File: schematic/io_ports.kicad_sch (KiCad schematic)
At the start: 4 parts, among them J1 Cartridge Port, J2 Expansion Port

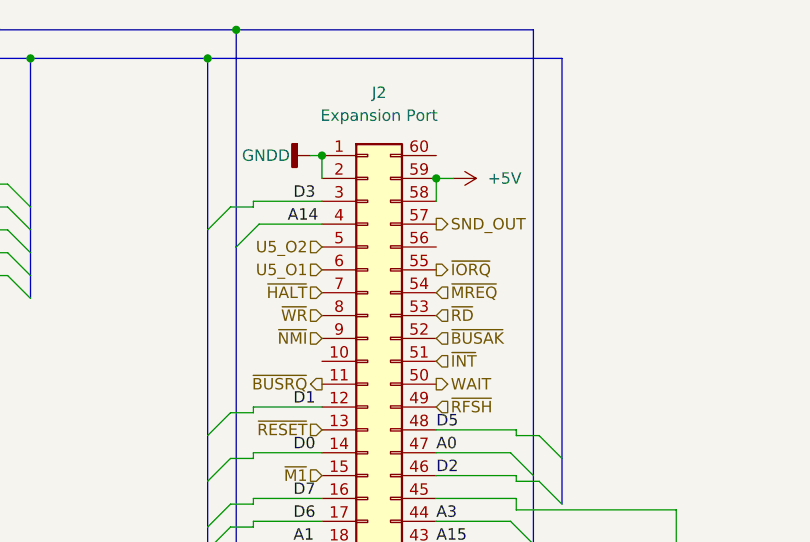
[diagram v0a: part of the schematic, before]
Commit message: power supply added, controller circuit added. Controller is a very odd duck to say the least. Seems they wanted to have plenty of current, maybe due to the steering wheel attachement?
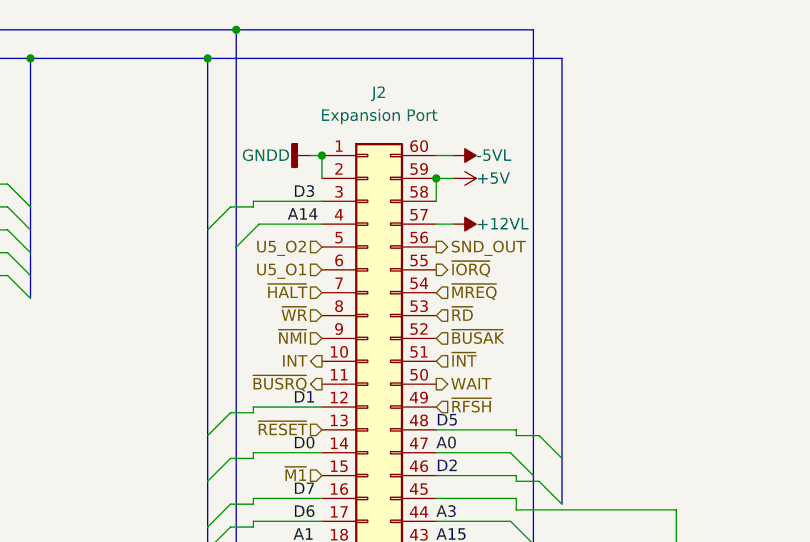
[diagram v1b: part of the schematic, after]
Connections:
- net SND_OUT: now also J2.56 (Pin_56); no longer J2.57 (Pin_57)
- net INT: now reaches J2.10 (Pin_10)
- net -5VL: now reaches J2.60 (Pin_60)
- new net +12VL: J2.57 (Pin_57)
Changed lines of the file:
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@@
+    (stroke (width 0) (type default) (color 0 0 0 0))
+  )
+  (wire (pts (xy 177.8 54.61) (xy 175.895 54.61))
     (stroke (width 0) (type default) (color 0 0 0 0))
   )
@@
     (stroke (width 0) (type default) (color 0 0 0 0))
   )
+  (wire (pts (xy 175.895 46.99) (xy 177.8 46.99))
+    (stroke (width 0) (type default) (color 0 0 0 0))
+  )
   (bus (pts (xy 153.67 102.87) (xy 153.67 105.41))
     (stroke (width 0) (type default) (color 0 0 0 0))
@@
     (effects (font (size 1.27 1.27)) (justify right))
   )
+  (hierarchical_label "INT" (shape output) (at 163.195 69.85 180)
+    (effects (font (size 1.27 1.27)) (justify right))
+  )
   (hierarchical_label "E3_U5" (shape output) (at 144.145 118.745 180)
     (effects (font (size 1.27 1.27)) (justify right))
@@
     (effects (font (size 1.27 1.27)) (justify left))
   )
-  (hierarchical_label "SND_OUT" (shape output) (at 175.895 54.61 0)
+  (hierarchical_label "SND_OUT" (shape output) (at 175.895 57.15 0)
     (effects (font (size 1.27 1.27)) (justify left))
   )
@@
   )
   (symbol (lib_id "power:+5V") (at 177.8 49.53 270) (unit 1)
-    (in_bom yes) (on_board yes) (fields_autoplaced)
+    (in_bom yes) (on_board yes)
     (property "Reference" "#PWR?" (id 0) (at 173.99 49.53 0)
       (effects (font (size 1.27 1.27)) hide)
     )
-    (property "Value" "+5V" (id 1) (at 181.61 49.5299 90)
+    (property "Value" "+5V" (id 1) (at 180.34 49.53 90)
       (effects (font (size 1.27 1.27)) (justify left))
     )
@@
     (pin "2")
   )
+  (symbol (lib_id "Power_Symbols:-5VL") (at 177.8 46.99 270) (unit 1)
+    (in_bom yes) (on_board yes)
+    (property "Reference" "#PWR?" (id 0) (at 180.34 46.99 0)
+      (effects (font (size 1.27 1.27)) hide)
+    )
+    (property "Value" "-5VL" (id 1) (at 180.34 46.99 90)
+      (effects (font (size 1.27 1.27)) (justify left))
+    )
+    (property "Footprint" "" (id 2) (at 177.8 46.99 0)
+      (effects (font (size 1.27 1.27)) hide)
+    )
+    (property "Datasheet" "" (id 3) (at 177.8 46.99 0)
+      (effects (font (size 1.27 1.27)) hide)
+    )
+    (pin "1")
+  )
   (symbol (lib_id "power:+5V") (at 117.475 83.185 180) (unit 1)
     (in_bom yes) (on_board yes) (fields_autoplaced)
@@
       (effects (font (size 1.27 1.27)) hide)
     )
+    (pin "1")
+  )
+  (symbol (lib_id "Power_Symbols:+12VL") (at 177.8 54.61 270) (unit 1)
+    (in_bom yes) (on_board yes)
+    (property "Reference" "#PWR?" (id 0) (at 180.34 54.61 0)
+      (effects (font (size 1.27 1.27)) hide)
+    )
+    (property "Value" "+12VL" (id 1) (at 180.34 54.61 90)
+      (effects (font (size 1.27 1.27)) (justify left))
+    )
+    (property "Footprint" "" (id 2) (at 177.8 54.61 0)
+      (effects (font (size 1.27 1.27)) hide)
+    )
+    (property "Datasheet" "" (id 3) (at 177.8 54.61 0)
+      (effects (font (size 1.27 1.27)) hide)
+    )

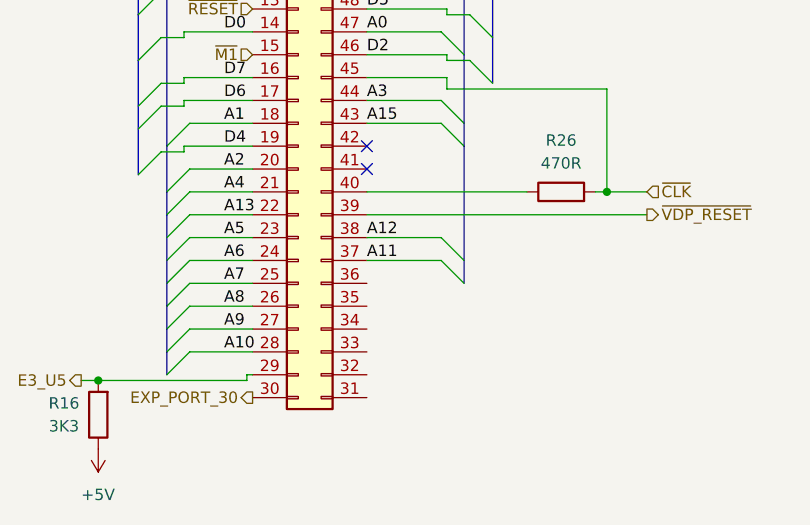
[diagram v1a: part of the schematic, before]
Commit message: started work on clock_reset_misc circuits. inverter u7 done, u8 added and starting work around U22.
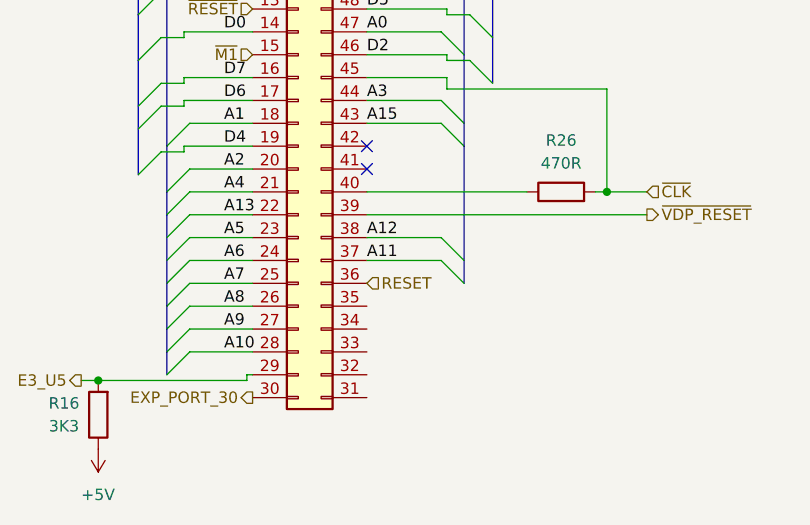
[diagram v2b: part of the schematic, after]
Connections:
- net RESET: now reaches J2.36 (Pin_36)
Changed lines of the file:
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@@
+    (effects (font (size 1.27 1.27)) (justify left))
+  )
+  (hierarchical_label "RESET" (shape input) (at 175.895 107.95 0)
     (effects (font (size 1.27 1.27)) (justify left))
   )

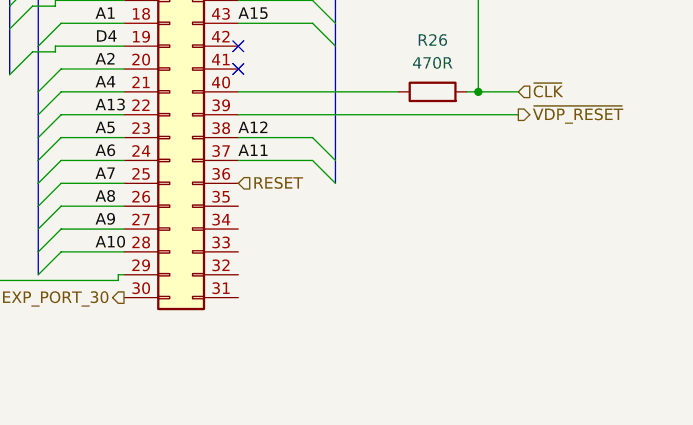
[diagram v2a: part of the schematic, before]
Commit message: altered and did some cleanup of the way the wires were run. Finished expansion port routes to rf modulator. Added ext_psu for future external power supply design (will be an off the shelf psu block).
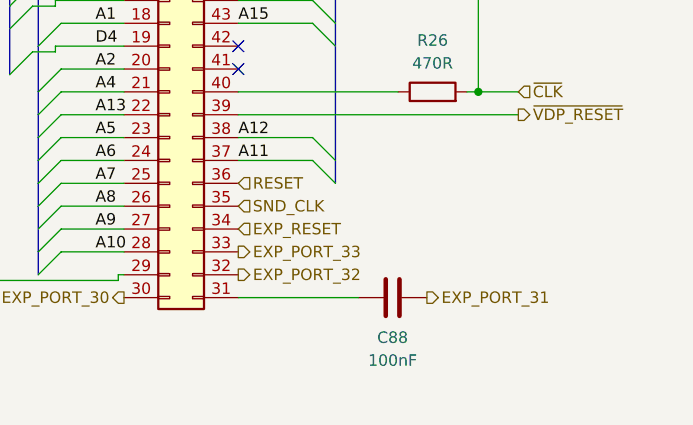
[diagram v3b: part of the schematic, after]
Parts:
- added C88: 100nF, symbol Device:C
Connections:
- net at J2.31 (Pin_31): now also C88.1
- net EXP_PORT_32: now reaches J2.32 (Pin_32)
- net EXP_PORT_33: now reaches J2.33 (Pin_33)
- net EXP_RESET: now reaches J2.34 (Pin_34)
- net SND_CLK: now reaches J2.35 (Pin_35)
- new net EXP_PORT_31: C88.2
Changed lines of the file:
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@@
+    (stroke (width 0) (type default) (color 0 0 0 0))
+  )
+  (wire (pts (xy 175.895 120.65) (xy 189.23 120.65))
     (stroke (width 0) (type default) (color 0 0 0 0))
   )
@@
     (effects (font (size 1.27 1.27)) (justify right))
   )
+  (hierarchical_label "EXP_PORT_32" (shape output) (at 175.895 118.11 0)
+    (effects (font (size 1.27 1.27)) (justify left))
+  )
   (hierarchical_label "~{NMI}" (shape input) (at 163.195 67.31 180)
     (effects (font (size 1.27 1.27)) (justify right))
@@
     (effects (font (size 1.27 1.27)) (justify right))
   )
+  (hierarchical_label "EXP_PORT_31" (shape output) (at 196.85 120.65 0)
+    (effects (font (size 1.27 1.27)) (justify left))
+  )
   (hierarchical_label "INT" (shape output) (at 163.195 69.85 180)
     (effects (font (size 1.27 1.27)) (justify right))
@@
     (effects (font (size 1.27 1.27)) (justify right))
   )
+  (hierarchical_label "EXP_RESET" (shape input) (at 175.895 113.03 0)
+    (effects (font (size 1.27 1.27)) (justify left))
+  )
   (hierarchical_label "U5_O4" (shape input) (at 117.475 67.945 0)
     (effects (font (size 1.27 1.27)) (justify left))
   )
+  (hierarchical_label "SND_CLK" (shape input) (at 175.895 110.49 0)
+    (effects (font (size 1.27 1.27)) (justify left))
+  )
   (hierarchical_label "~{CLK}" (shape input) (at 207.01 97.79 0)
+    (effects (font (size 1.27 1.27)) (justify left))
+  )
+  (hierarchical_label "EXP_PORT_33" (shape output) (at 175.895 115.57 0)
     (effects (font (size 1.27 1.27)) (justify left))
   )
@@
     (pin "1")
   )
+  (symbol (lib_id "Device:C") (at 193.04 120.65 90) (unit 1)
+    (in_bom yes) (on_board yes)
+    (property "Reference" "C88" (id 0) (at 193.04 125.095 90))
+    (property "Value" "100nF" (id 1) (at 193.04 127.635 90))
+    (property "Footprint" "" (id 2) (at 196.85 119.6848 0)
+      (effects (font (size 1.27 1.27)) hide)
+    )
+    (property "Datasheet" "~" (id 3) (at 193.04 120.65 0)
+      (effects (font (size 1.27 1.27)) hide)
+    )
+    (pin "1")
+    (pin "2")
+  )
   (symbol (lib_id "Power_Symbols:+12VL") (at 177.8 54.61 270) (unit 1)

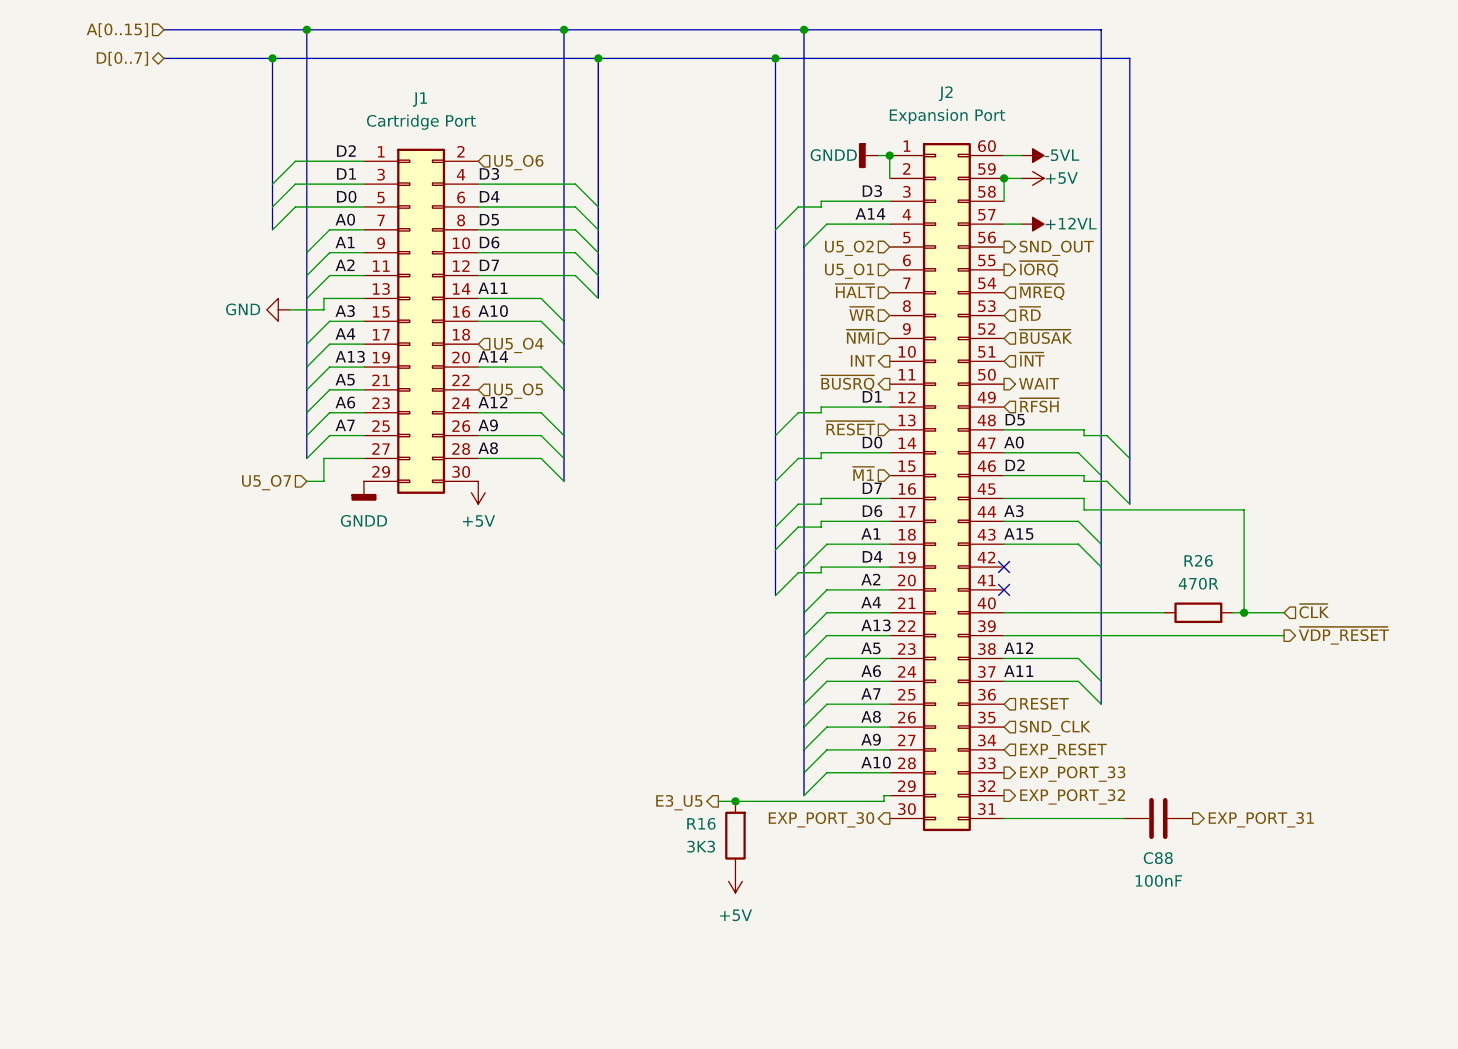
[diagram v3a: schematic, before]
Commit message: cleanup of power supply, and another pass at the RF circuit. Both look much better. The RF circuit just looks wrong though. Will need to check it over.
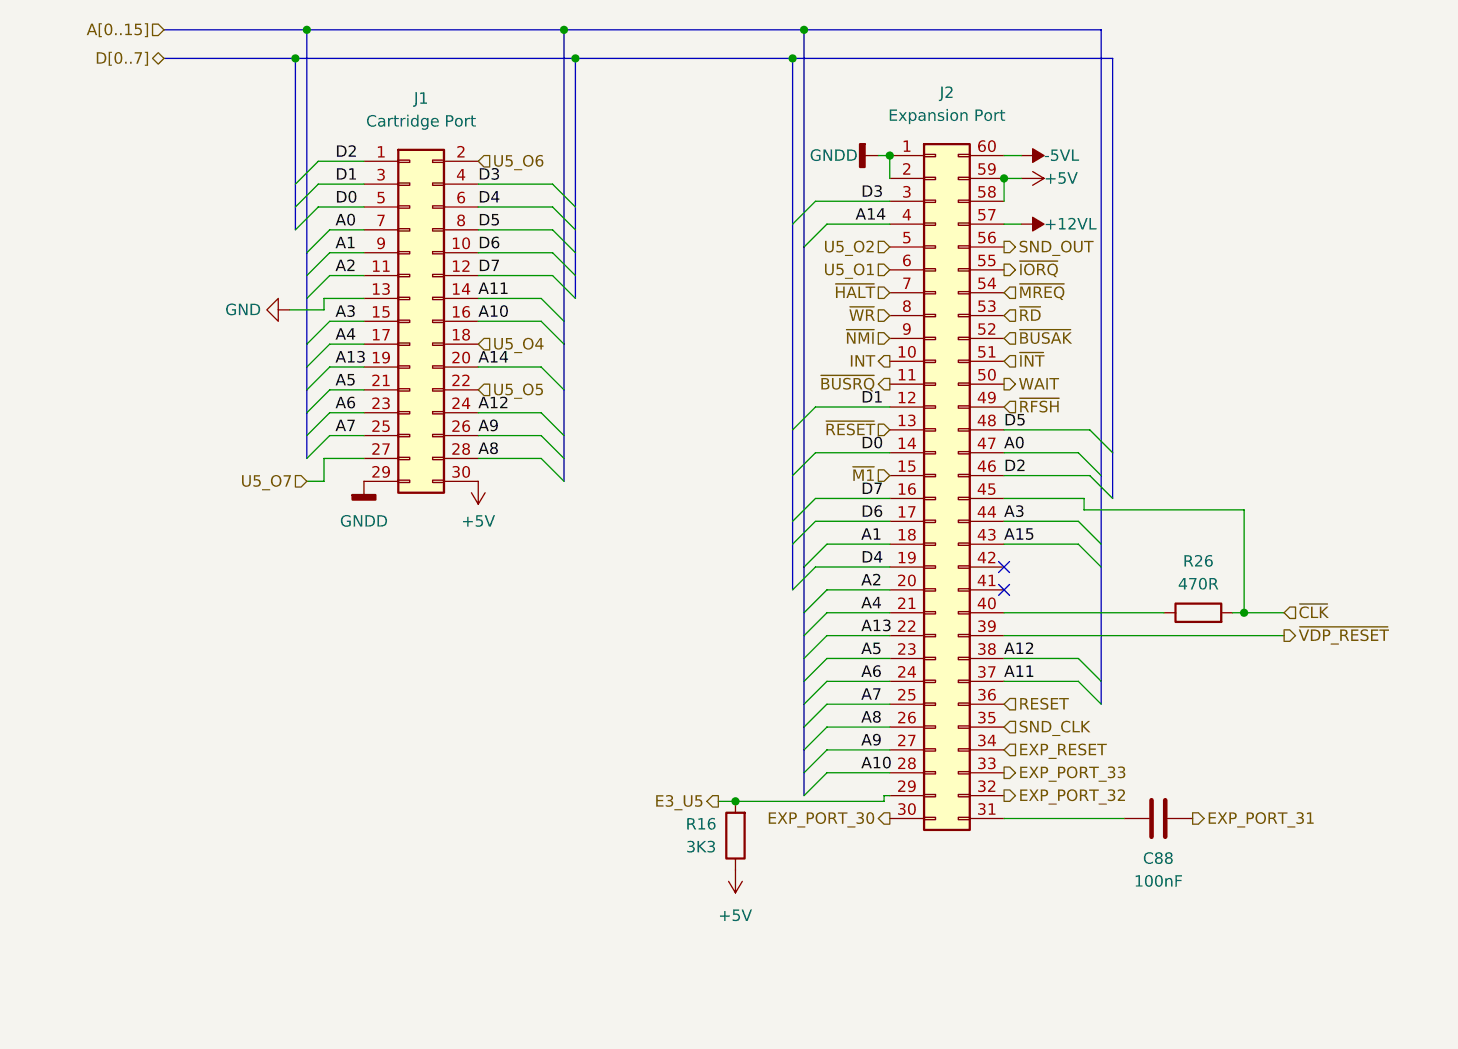
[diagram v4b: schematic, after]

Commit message: all lines renamed, based most of the names from the coleco adam schematic. CS cart lines are my own, and the rest are from the wiki schematic for the controller... those will need to be checked.
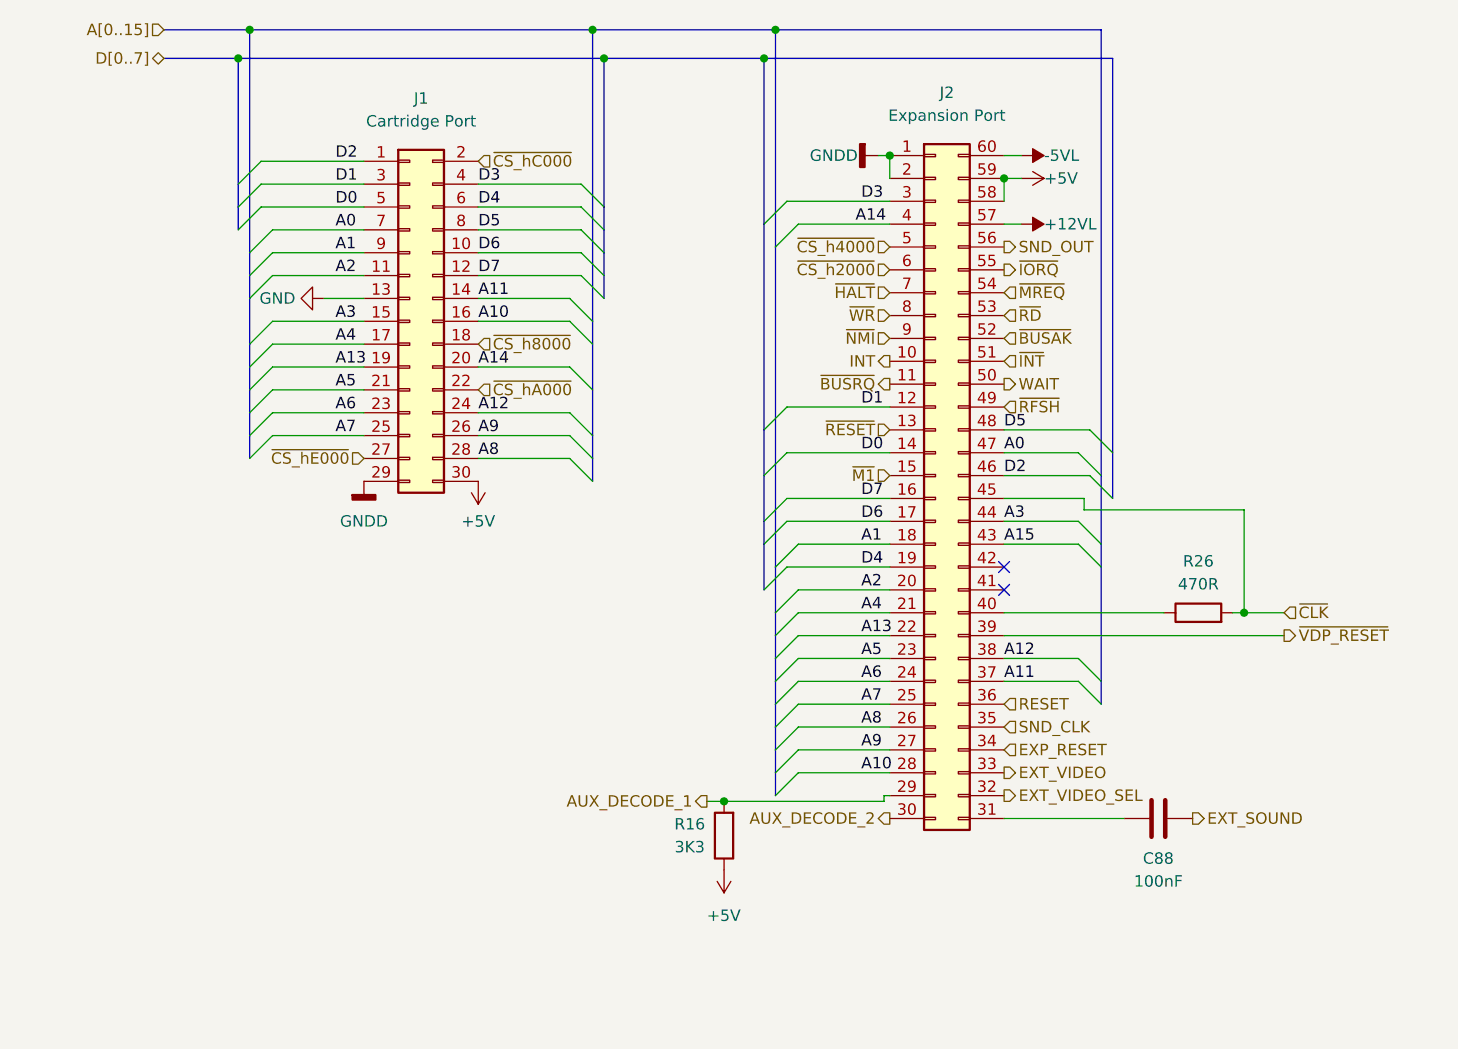
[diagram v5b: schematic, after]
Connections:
- net E3_U5 renamed AUX_DECODE_1
- net EXP_PORT_30 renamed AUX_DECODE_2
- net EXP_PORT_31 renamed EXT_SOUND
- net EXP_PORT_32 renamed EXT_VIDEO_SEL
- net EXP_PORT_33 renamed EXT_VIDEO
- net U5_O1 renamed ~{CS_h2000}
- net U5_O2 renamed ~{CS_h4000}
- net U5_O4 renamed ~{CS_h8000}
- net U5_O5 renamed ~{CS_hA000}
- net U5_O6 renamed ~{CS_hC000}
- net U5_O7 renamed ~{CS_hE000}
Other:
- moved on the sheet: R16
